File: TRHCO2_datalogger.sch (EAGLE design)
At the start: 64 parts, among them J3 MicroUSB (5V), T2 MMUN2133LT1G, U1 ATMEGA328P-MU, U2 FT231XQ-R, U3 DS3234, U4 TPS61090RSAR, U5 MCP73871, U6 K30-CO2-I2C, U7 SHT31/35, U8 MCP1703/3.3V, Y2 SPARKFUN_RESONATORSMD

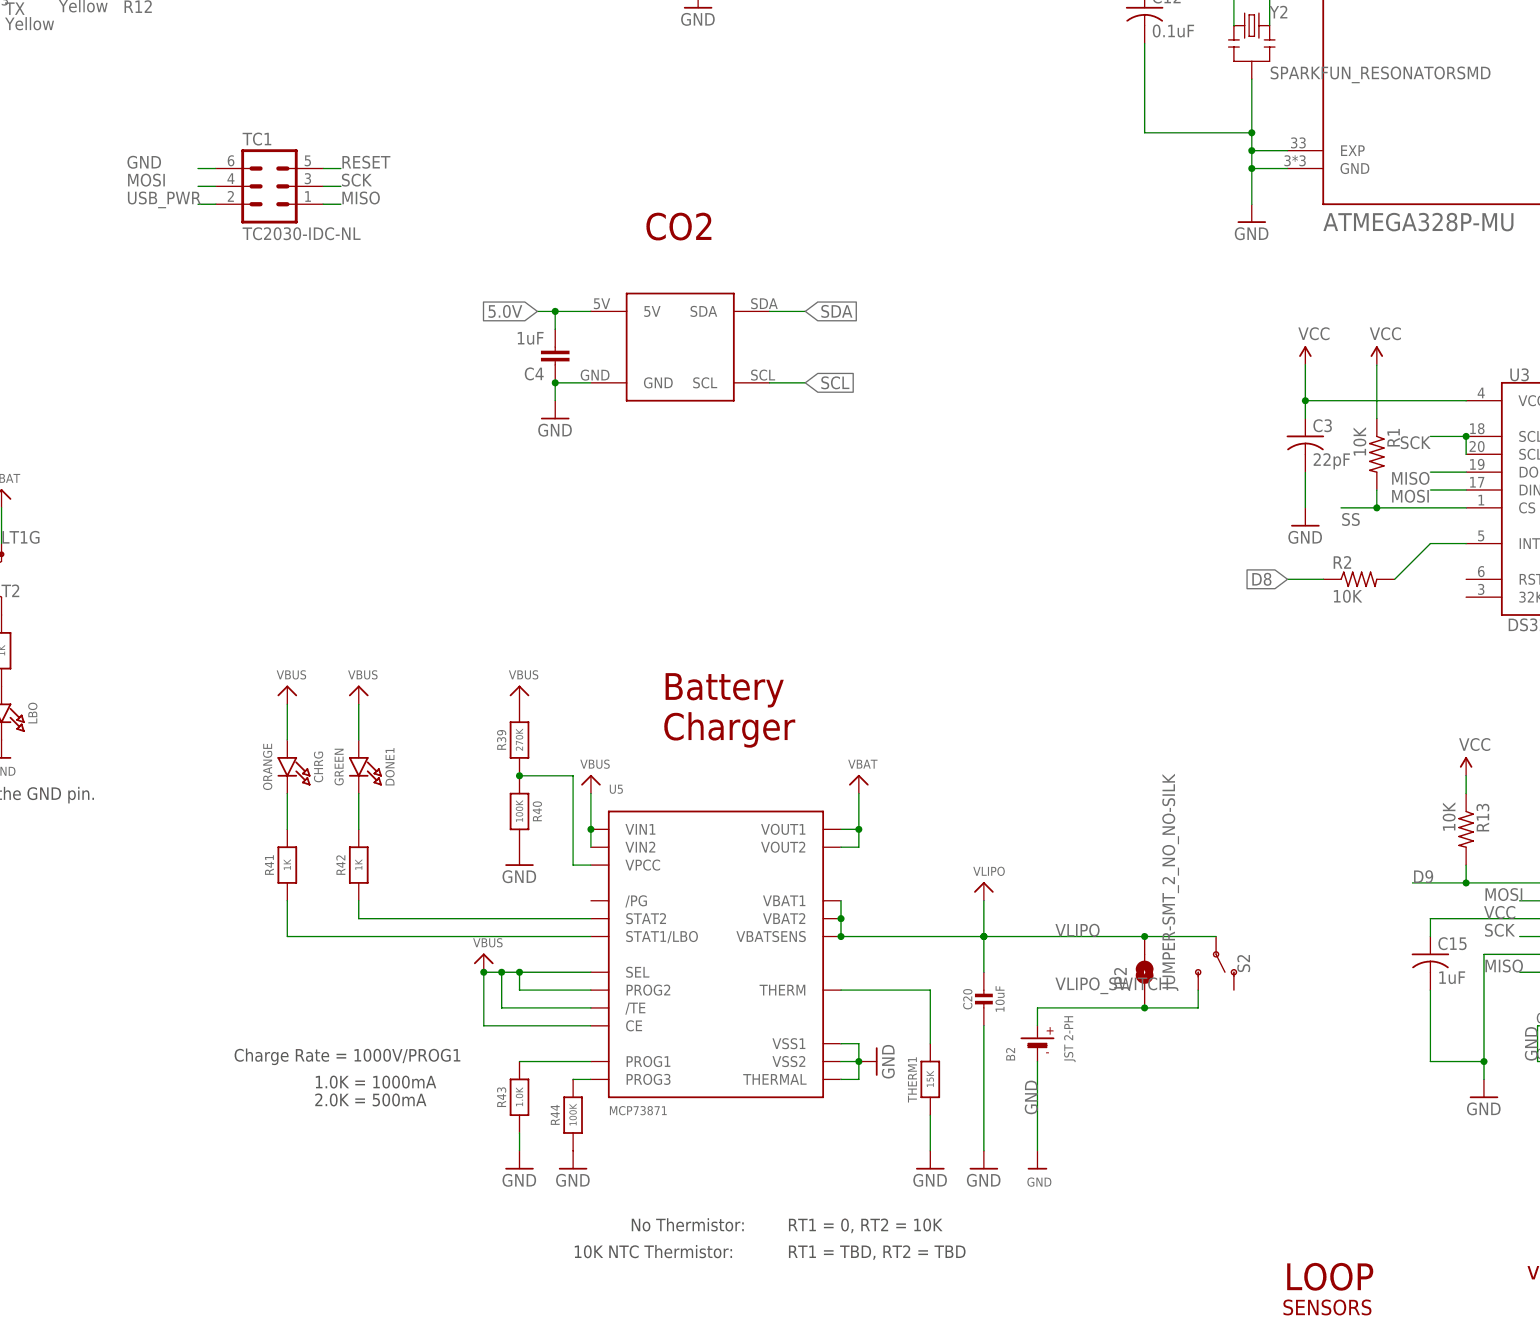
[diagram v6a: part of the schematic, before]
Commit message: Added power plane
Adjusted traces, added power planes, some other minor trace adjustments
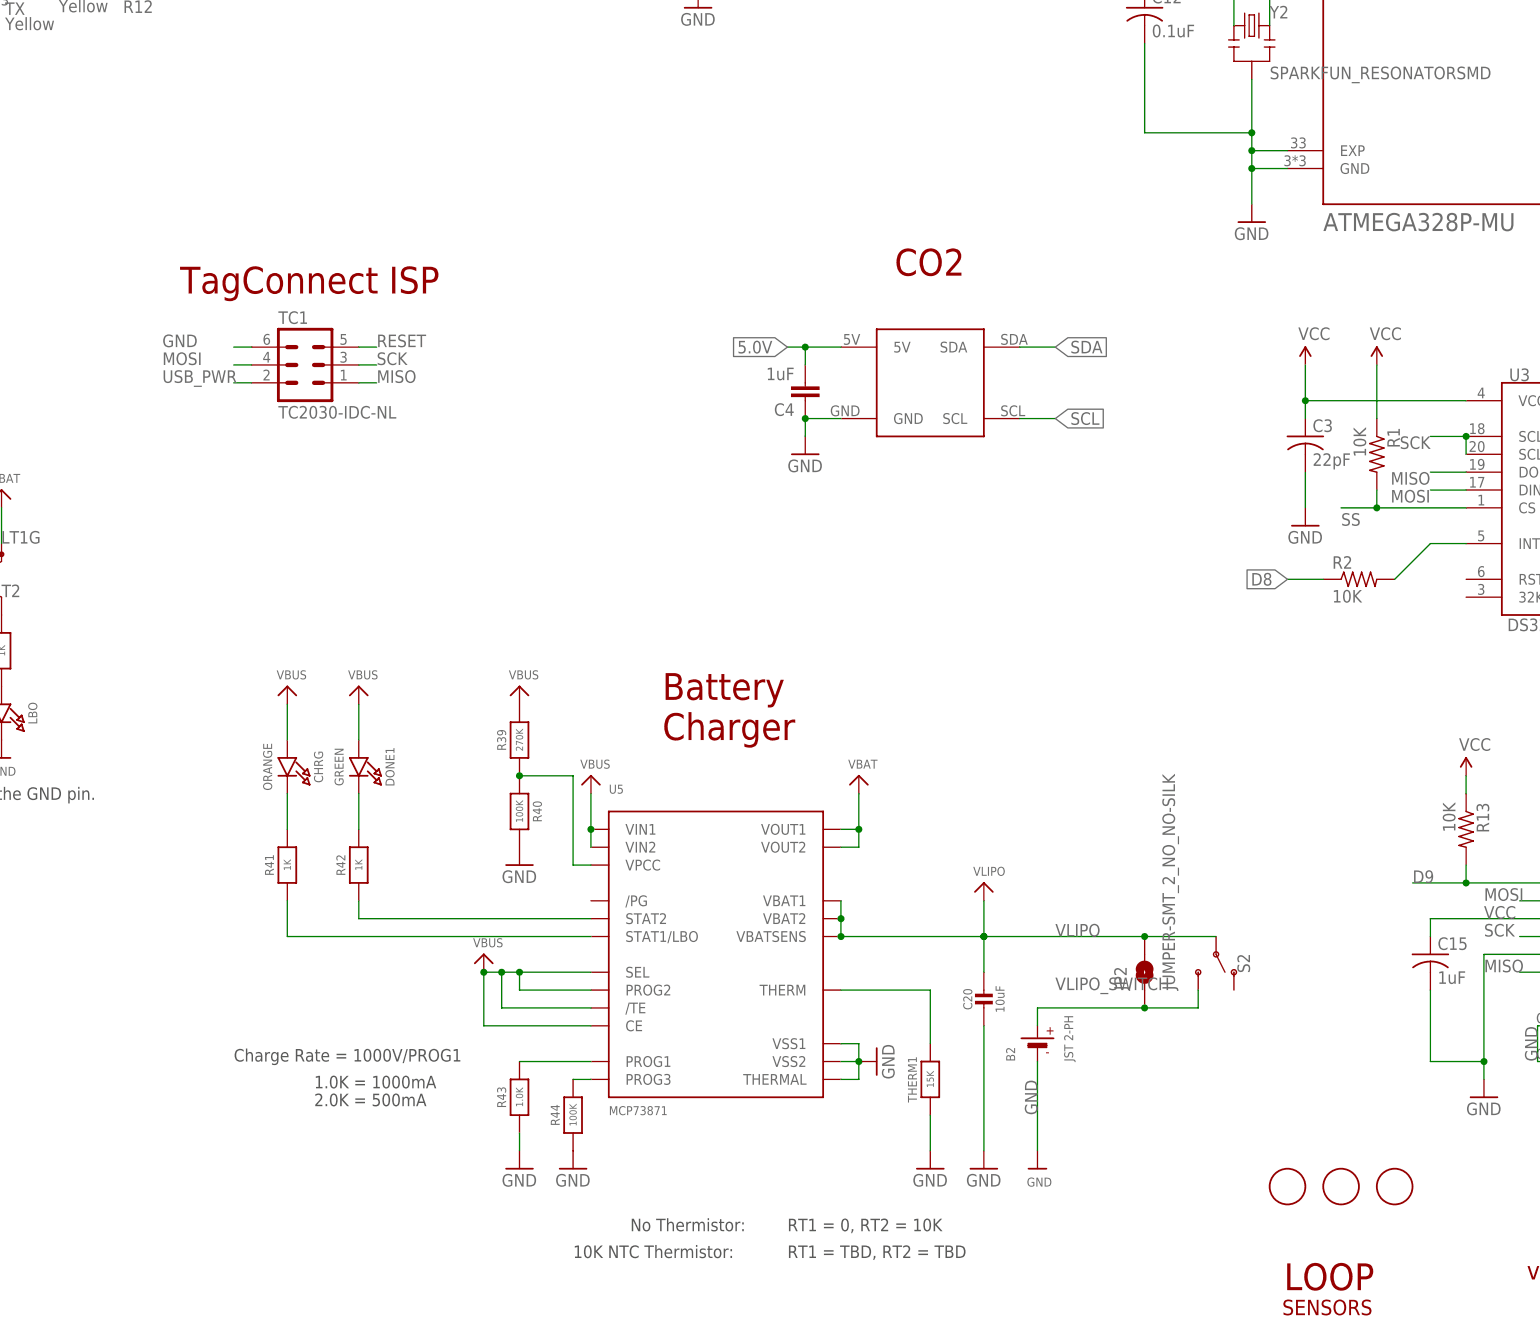
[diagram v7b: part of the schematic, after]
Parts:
- added U$1, U$2, U$3: FIDUCIAL, adafruit:FIDUCIAL
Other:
- note added: "TagConnect ISP"
- moved on the sheet: C4, TC1
